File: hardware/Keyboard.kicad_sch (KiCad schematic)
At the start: 28 parts, among them J1 USB_C_Receptacle_USB2.0_16P, J2 Conn_01x04, SW1 SW_Push, SW2 SW_Push, U1 XC6206PxxxMR, U2 STM32F072CBTx

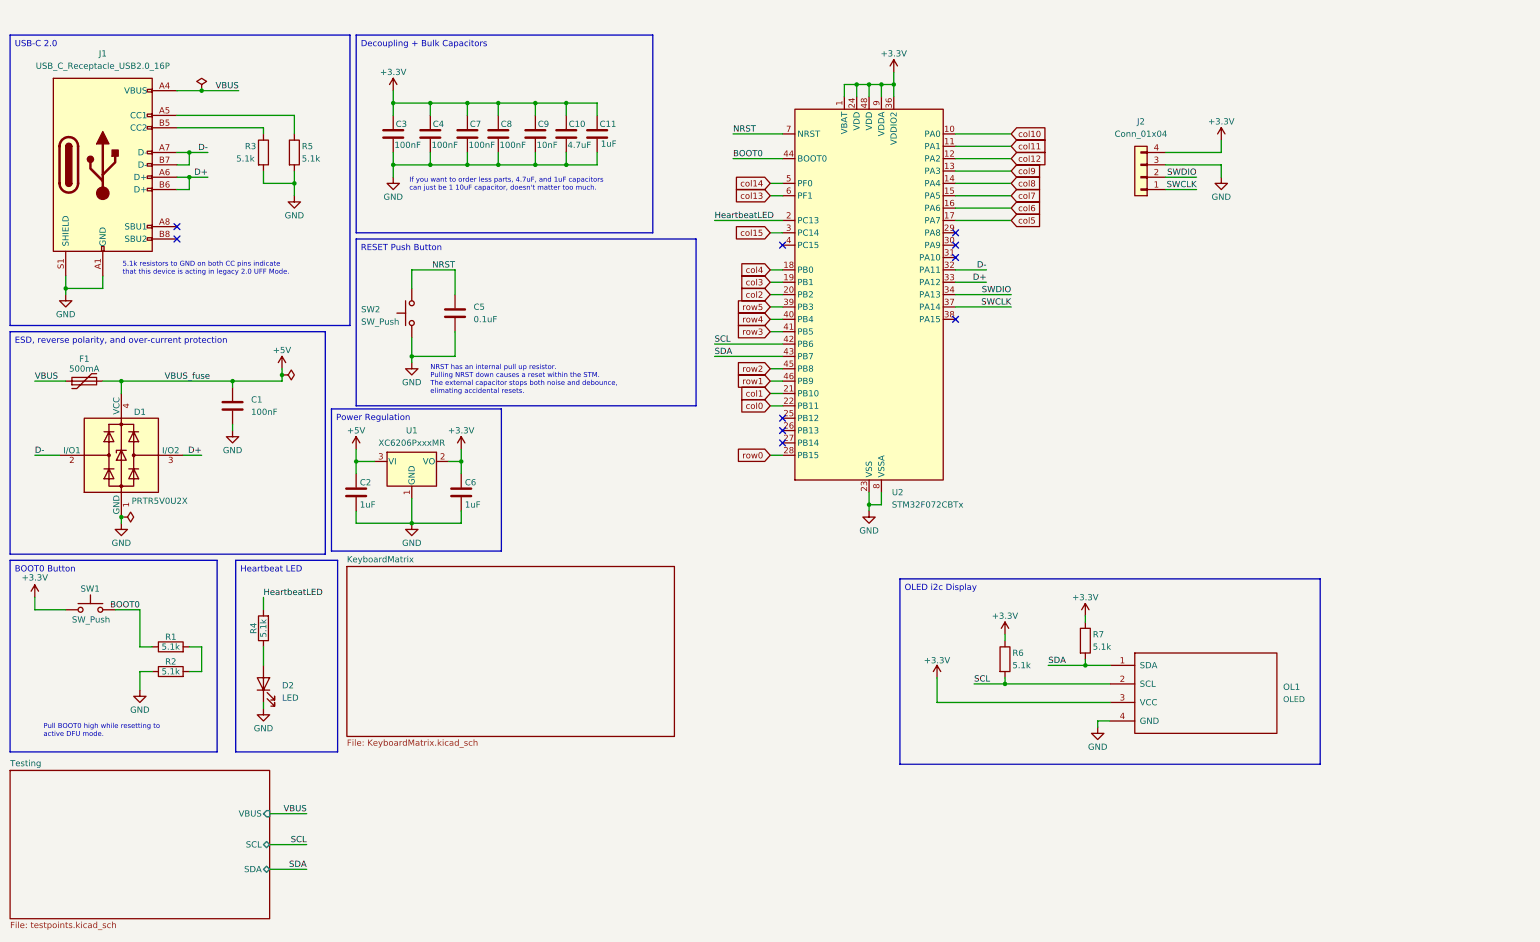
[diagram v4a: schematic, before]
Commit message: production files added --> ready for assembly
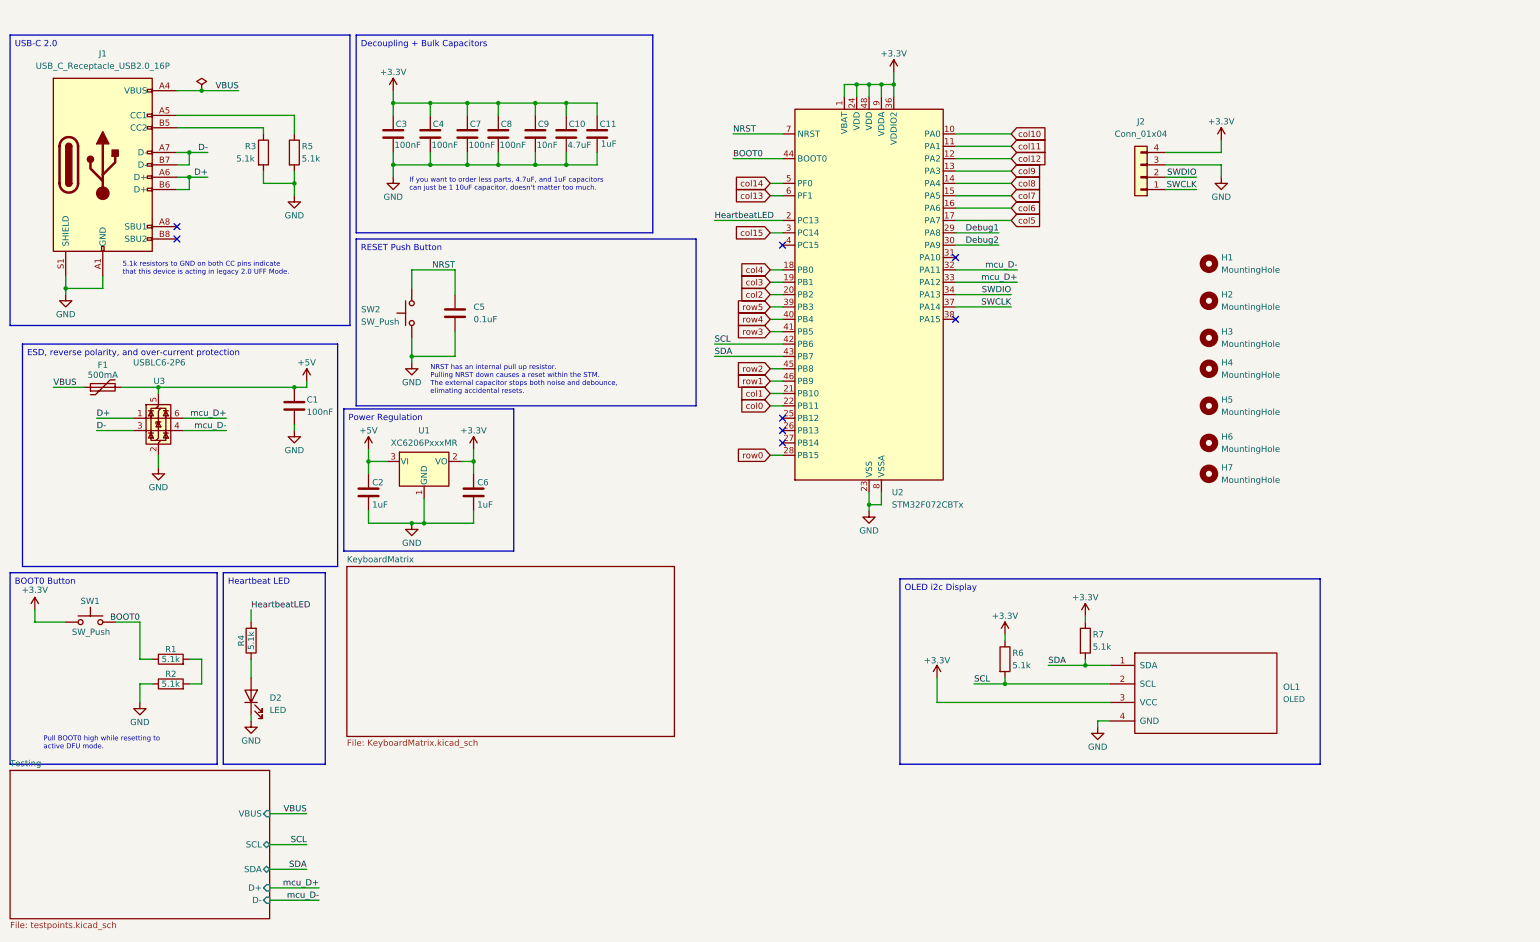
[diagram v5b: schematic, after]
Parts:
- removed D1: PRTR5V0U2X, Package_TO_SOT_SMD:SOT-143, symbol Power_Protection:PRTR5V0U2X
- added H1, H2, H3, H4, H5, H6, H7: MountingHole, MountingHole:MountingHole_3.2mm_M3_ISO7380, symbol Mechanical:MountingHole
- added U3: USBLC6-2P6, Package_TO_SOT_SMD:SOT-666, symbol Power_Protection:USBLC6-2P6
- F1: P/N (none) -> 0603L050YR
- J1: footprint PCM_marbastlib-various:USB_C_Receptacle_HRO_TYPE-C-31-M-23 -> Connector_USB:USB_C_Receptacle_GCT_USB4105-xx-A_16P_TopMnt_Horizontal; P/N (none) -> 640-USB4105-GF-A
- J2, OL1: now left out of the parts list
- SW1, SW2: P/N (none) -> 688-SKRKAG
- U2: P/N (none) -> STM32F072CBT6
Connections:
- net +5V: now also U3.5 (VBUS)
- net D+: now also U3.1 (I/O1); no longer U2.33 (PA12)
- net D-: now also U3.3 (I/O2); no longer U2.32 (PA11)
- net GND: now also U3.2 (GND)
- net Debug1: now reaches U2.29 (PA8)
- net Debug2: now reaches U2.30 (PA9)
- new net mcu_D+: U2.33 (PA12), U3.6 (I/O1)
- new net mcu_D-: U2.32 (PA11), U3.4 (I/O2)
- no-connect marks 10 -> 8
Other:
- sheet Testing ports: added D+, D-; removed none
- moved on the sheet: C2, C6, D2, R1, R2, R4, SW1, U1
